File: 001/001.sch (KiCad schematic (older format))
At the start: 9 parts, among them J1 I2C 5V, J2 I2C 5V, J3 I2C 5V, J4 I2C 3.3V, J5 I2C 3.3V

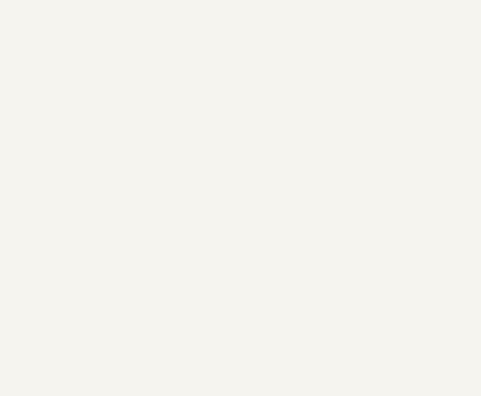
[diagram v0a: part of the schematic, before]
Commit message: sche: Jack-DCを追加
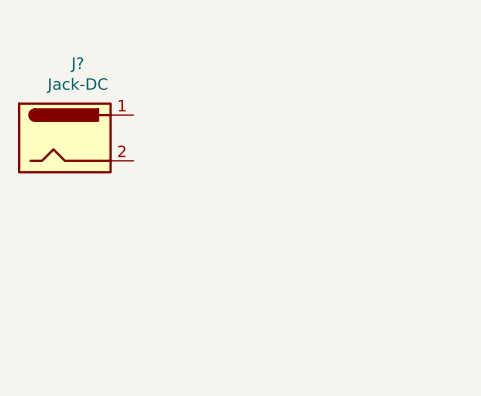
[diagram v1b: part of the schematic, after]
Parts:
- added J?: Jack-DC, symbol Connector:Jack-DC
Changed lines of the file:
@@
+	1    0    0    -1
+$EndComp
+$Comp
+L Connector:Jack-DC J?
+U 1 1 5F68DAE2
+P 2100 1500
+F 0 "J?" H 2157 1825 50  0000 C CNN
+F 1 "Jack-DC" H 2157 1734 50  0000 C CNN
+F 2 "" H 2150 1460 50  0001 C CNN
+F 3 "~" H 2150 1460 50  0001 C CNN
+	1    2100 1500
 	1    0    0    -1
 $EndComp
